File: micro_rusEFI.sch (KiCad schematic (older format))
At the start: 59 parts, among them J10 Conn_01x01, J11 Conn_01x01, J12 Conn_01x01, J13 Conn_01x01, J14 Conn_01x01, J16 Conn_01x01, J3 Conn_01x01, J4 Conn_02x05_Counter_Clockwise, J5 Conn_01x01, J6 Conn_01x01, J8 Conn_01x01, J9 Conn_01x01, U3 molex_48pin_MRE, U7 XC6206 3.3V

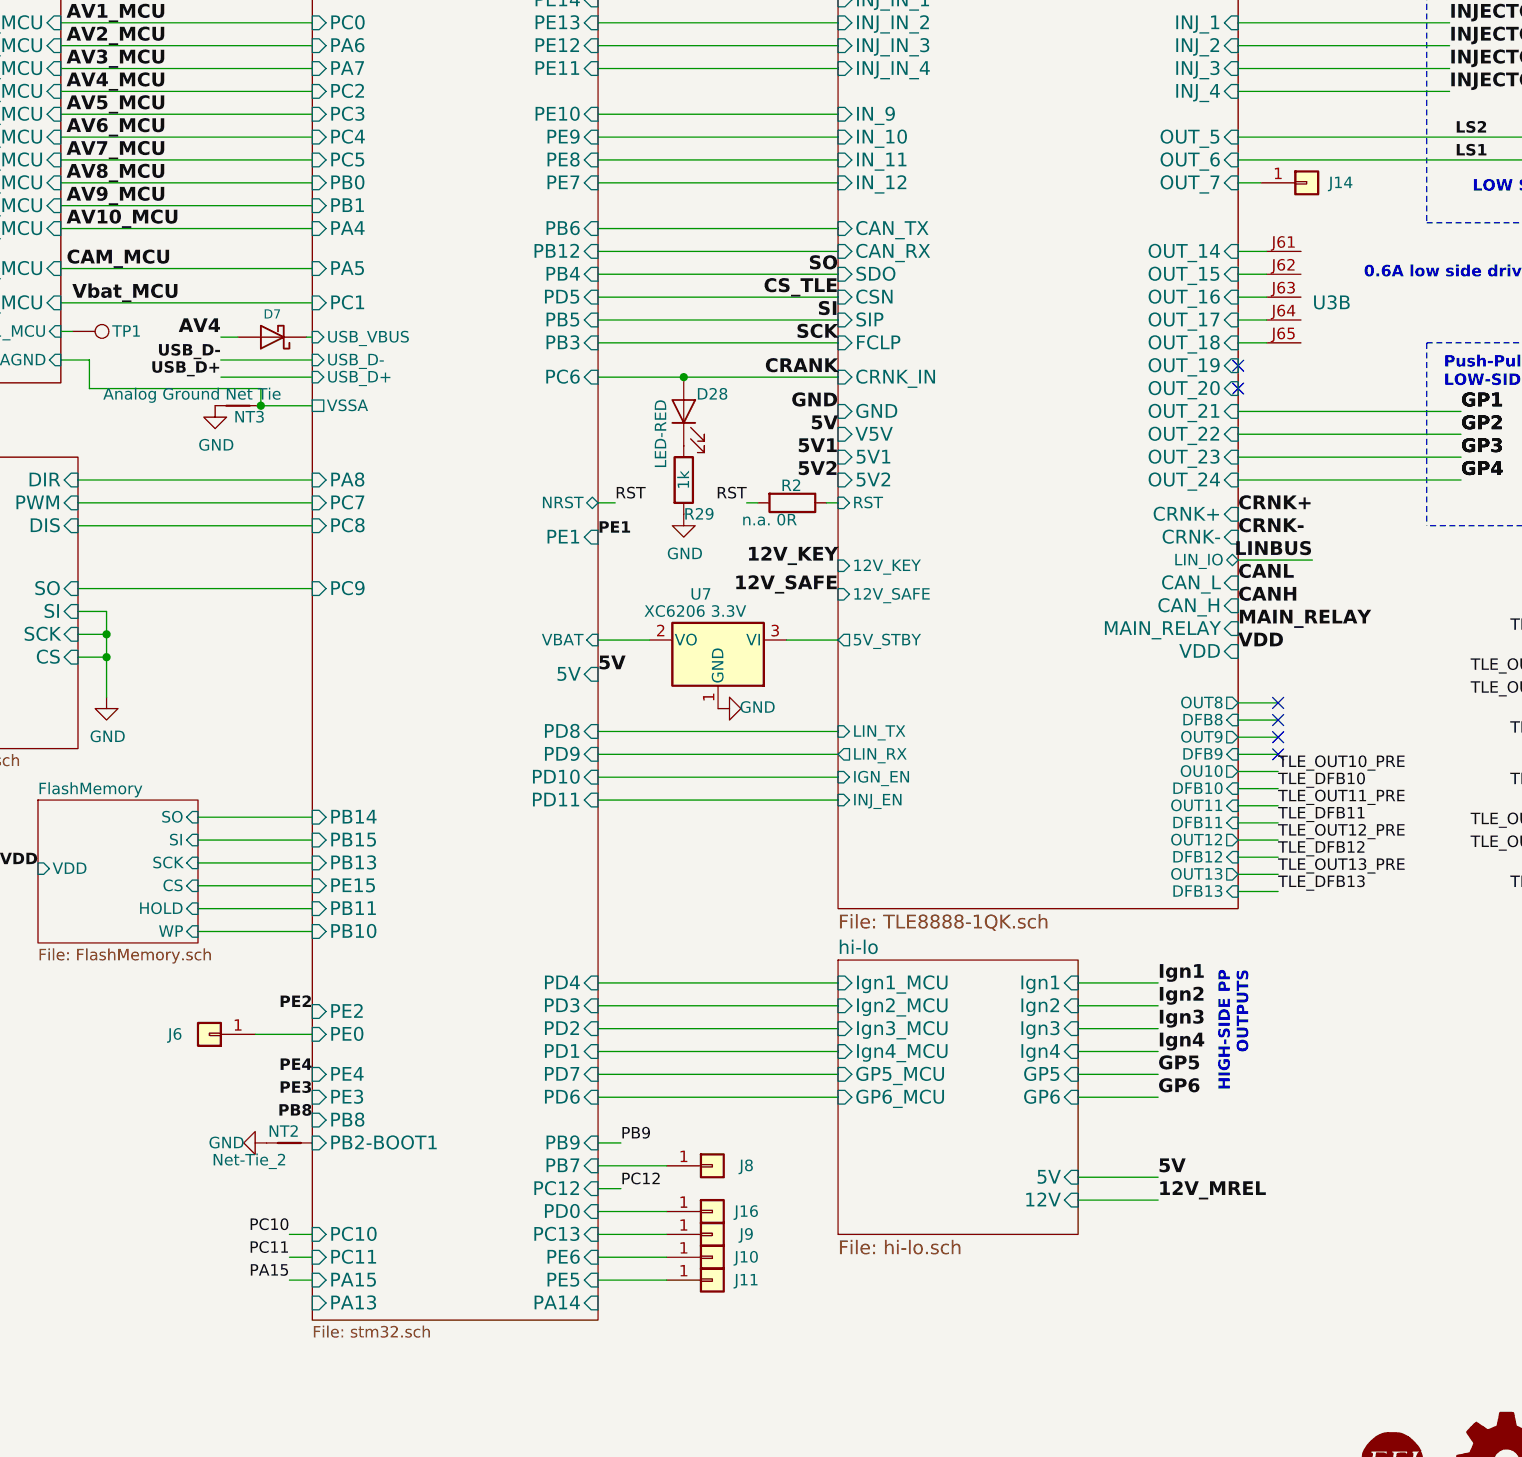
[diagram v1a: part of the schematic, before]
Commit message: Updated MRE footprint
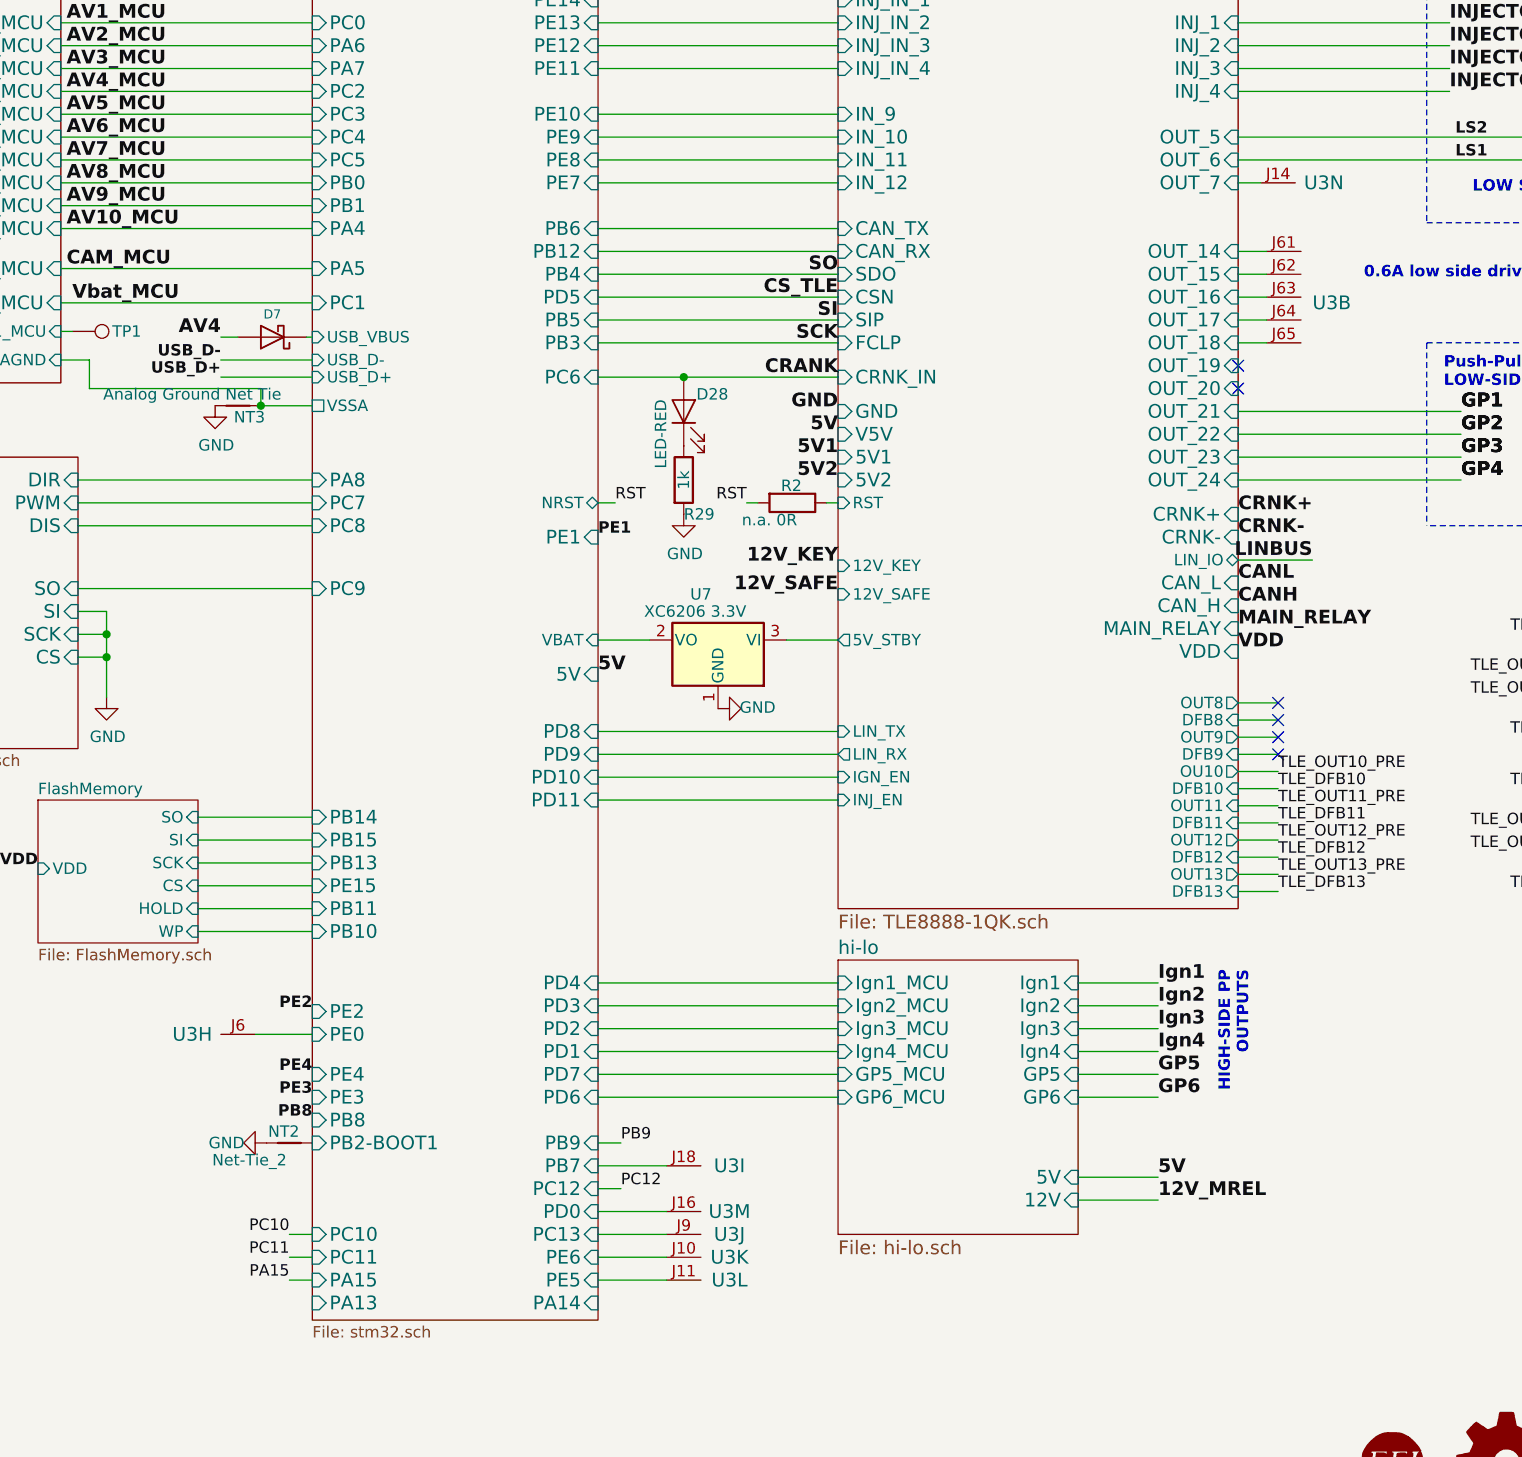
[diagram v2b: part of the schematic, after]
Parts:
- removed J10, J11, J14, J16, J6, J8, J9: Conn_01x01, Connector_Pin:Pin_D0.7mm_L6.5mm_W1.8mm_FlatFork, symbol Connector_Generic:Conn_01x01
- added unit 8 of U3
- added unit 9 of U3
- added unit 10 of U3
- added unit 11 of U3
- added unit 12 of U3
- added unit 13 of U3
- added unit 14 of U3
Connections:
- net MCU/PB7: now also U3.J18
- net MCU/PC13: now also U3.J9
- net MCU/PD0: now also U3.J16
- net MCU/PE0: now also U3.J6
- net MCU/PE5: now also U3.J11
- net MCU/PE6: now also U3.J10
- net TLE8888-1QK/OUT_7: now also U3.J14
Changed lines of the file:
@@
 F5 "OUT2" O R 13275 7550 50
 $EndSheet
-$Comp
-L Connector_Generic:Conn_01x01 J8
-U 1 1 5F20C313
-P 8450 8925
-F 0 "J8" H 8600 8925 50  0000 C CNN
-F 1 "Conn_01x01" H 8368 8791 50  0001 C CNN
-F 2 "Connector_Pin:Pin_D0.7mm_L6.5mm_W1.8mm_FlatFork" H 8450 8925 50  0001 C CNN
-F 3 "~" H 8450 8925 50  0001 C CNN
-	1    8450 8925
-	1    0    0    -1
-$EndComp
 Wire Wire Line
 	7950 8925 8250 8925
-$Comp
-L Connector_Generic:Conn_01x01 J6
-U 1 1 5F21FF07
-P 6250 8350
-F 0 "J6" H 6400 8350 50  0000 C CNN
-F 1 "Conn_01x01" H 6168 8216 50  0001 C CNN
-F 2 "Connector_Pin:Pin_D0.7mm_L6.5mm_W1.8mm_FlatFork" H 6250 8350 50  0001 C CNN
-F 3 "~" H 6250 8350 50  0001 C CNN
-	1    6250 8350
-	-1   0    0    1
-$EndComp
 Wire Wire Line
 	6700 8350 6450 8350
-$Comp
-L Connector_Generic:Conn_01x01 J10
-U 1 1 5F231677
-P 8450 9325
-F 0 "J10" H 8600 9325 50  0000 C CNN
-F 1 "Conn_01x01" H 8368 9191 50  0001 C CNN
-F 2 "Connector_Pin:Pin_D0.7mm_L6.5mm_W1.8mm_FlatFork" H 8450 9325 50  0001 C CNN
-F 3 "~" H 8450 9325 50  0001 C CNN
-	1    8450 9325
-	1    0    0    -1
-$EndComp
-$Comp
-L Connector_Generic:Conn_01x01 J11
-U 1 1 5F231C34
-P 8450 9425
-F 0 "J11" H 8600 9425 50  0000 C CNN
-F 1 "Conn_01x01" H 8368 9291 50  0001 C CNN
-F 2 "Connector_Pin:Pin_D0.7mm_L6.5mm_W1.8mm_FlatFork" H 8450 9425 50  0001 C CNN
-F 3 "~" H 8450 9425 50  0001 C CNN
-	1    8450 9425
-	1    0    0    -1
-$EndComp
 Wire Wire Line
 	7950 9325 8250 9325
 Wire Wire Line
 	7950 9425 8250 9425
-$Comp
-L Connector_Generic:Conn_01x01 J9
-U 1 1 5F2548AA
-P 8450 9225
-F 0 "J9" H 8600 9225 50  0000 C CNN
-F 1 "Conn_01x01" H 8368 9091 50  0001 C CNN
-F 2 "Connector_Pin:Pin_D0.7mm_L6.5mm_W1.8mm_FlatFork" H 8450 9225 50  0001 C CNN
-F 3 "~" H 8450 9225 50  0001 C CNN
-	1    8450 9225
-	1    0    0    -1
-$EndComp
 Wire Wire Line
 	7950 9225 8250 9225
@@
 Wire Wire Line
 	13275 5125 13275 5025
-$Comp
-L Connector_Generic:Conn_01x01 J16
-U 1 1 5F3E511F
-P 8450 9125
-F 0 "J16" H 8600 9125 50  0000 C CNN
-F 1 "Conn_01x01" H 8368 8991 50  0001 C CNN
-F 2 "Connector_Pin:Pin_D0.7mm_L6.5mm_W1.8mm_FlatFork" H 8450 9125 50  0001 C CNN
-F 3 "~" H 8450 9125 50  0001 C CNN
-	1    8450 9125
-	1    0    0    -1
-$EndComp
 Wire Wire Line
 	7950 9125 8250 9125
@@
 Wire Wire Line
 	8600 6025 8650 6025
-$Comp
-L Connector_Generic:Conn_01x01 J14
-U 1 1 5EF49354
-P 11050 4625
-F 0 "J14" H 11200 4625 50  0000 C CNN
-F 1 "Conn_01x01" H 10968 4491 50  0001 C CNN
-F 2 "Connector_Pin:Pin_D0.7mm_L6.5mm_W1.8mm_FlatFork" H 11050 4625 50  0001 C CNN
-F 3 "~" H 11050 4625 50  0001 C CNN
-	1    11050 4625
-	1    0    0    -1
-$EndComp
 Wire Wire Line
 	10750 4625 10850 4625
@@
 	1    0    0    -1
 $EndComp
+$Comp
+L rusefi_Molex_MRE_Connector:molex_48pin_MRE U3
+U 8 1 5FDEA88F
+P 7000 8350
+F 0 "U3" H 7825 8350 60  0000 C CNN
+F 1 "molex_48pin_MRE" V 8181 8755 60  0001 C CNN
+F 2 "rusefi_lib:Molex_48_MRE" H 7000 8350 60  0001 C CNN
+F 3 "" H 7000 8350 60  0001 C CNN
+	8    7000 8350
+	-1   0    0    1
+$EndComp
+$Comp
+L rusefi_Molex_MRE_Connector:molex_48pin_MRE U3
+U 9 1 5FE1BBB9
+P 7700 8925
+F 0 "U3" H 8525 8925 60  0000 C CNN
+F 1 "molex_48pin_MRE" V 8881 9330 60  0001 C CNN
+F 2 "rusefi_lib:Molex_48_MRE" H 7700 8925 60  0001 C CNN
+F 3 "" H 7700 8925 60  0001 C CNN
+	9    7700 8925
+	1    0    0    -1
+$EndComp
+$Comp
+L rusefi_Molex_MRE_Connector:molex_48pin_MRE U3
+U 10 1 5FE33973
+P 7700 9225
+F 0 "U3" H 8525 9225 60  0000 C CNN
+F 1 "molex_48pin_MRE" V 8881 9630 60  0001 C CNN
+F 2 "rusefi_lib:Molex_48_MRE" H 7700 9225 60  0001 C CNN
+F 3 "" H 7700 9225 60  0001 C CNN
+	10   7700 9225
+	1    0    0    -1
+$EndComp
+$Comp
+L rusefi_Molex_MRE_Connector:molex_48pin_MRE U3
+U 11 1 5FE3397D
+P 7700 9325
+F 0 "U3" H 8525 9325 60  0000 C CNN
+F 1 "molex_48pin_MRE" V 8881 9730 60  0001 C CNN
+F 2 "rusefi_lib:Molex_48_MRE" H 7700 9325 60  0001 C CNN
+F 3 "" H 7700 9325 60  0001 C CNN
+	11   7700 9325
+	1    0    0    -1
+$EndComp
+$Comp
+L rusefi_Molex_MRE_Connector:molex_48pin_MRE U3
+U 12 1 5FE4FA20
+P 7700 9425
+F 0 "U3" H 8525 9425 60  0000 C CNN
+F 1 "molex_48pin_MRE" V 8881 9830 60  0001 C CNN
+F 2 "rusefi_lib:Molex_48_MRE" H 7700 9425 60  0001 C CNN
+F 3 "" H 7700 9425 60  0001 C CNN
+	12   7700 9425
+	1    0    0    -1
+$EndComp
+$Comp
+L rusefi_Molex_MRE_Connector:molex_48pin_MRE U3
+U 13 1 5FE4FA2A
+P 7700 9125
+F 0 "U3" H 8525 9125 60  0000 C CNN
+F 1 "molex_48pin_MRE" V 8881 9530 60  0001 C CNN
+F 2 "rusefi_lib:Molex_48_MRE" H 7700 9125 60  0001 C CNN
+F 3 "" H 7700 9125 60  0001 C CNN
+	13   7700 9125
+	1    0    0    -1
+$EndComp
+$Comp
+L rusefi_Molex_MRE_Connector:molex_48pin_MRE U3
+U 14 1 5FE4FA34
+P 10300 4625
+F 0 "U3" H 11125 4625 60  0000 C CNN
+F 1 "molex_48pin_MRE" V 11481 5030 60  0001 C CNN
+F 2 "rusefi_lib:Molex_48_MRE" H 10300 4625 60  0001 C CNN
+F 3 "" H 10300 4625 60  0001 C CNN
+	14   10300 4625
+	1    0    0    -1
+$EndComp

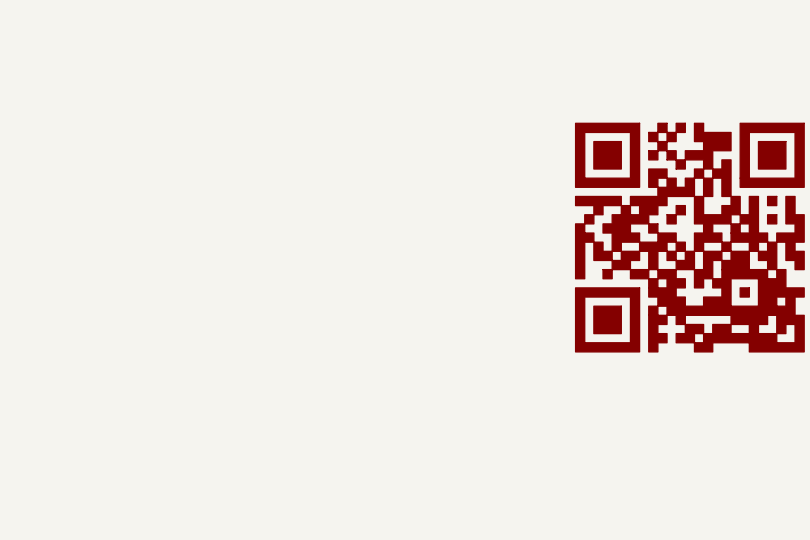
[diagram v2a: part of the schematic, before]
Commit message: Added disclaimer silk screen and schematic note.
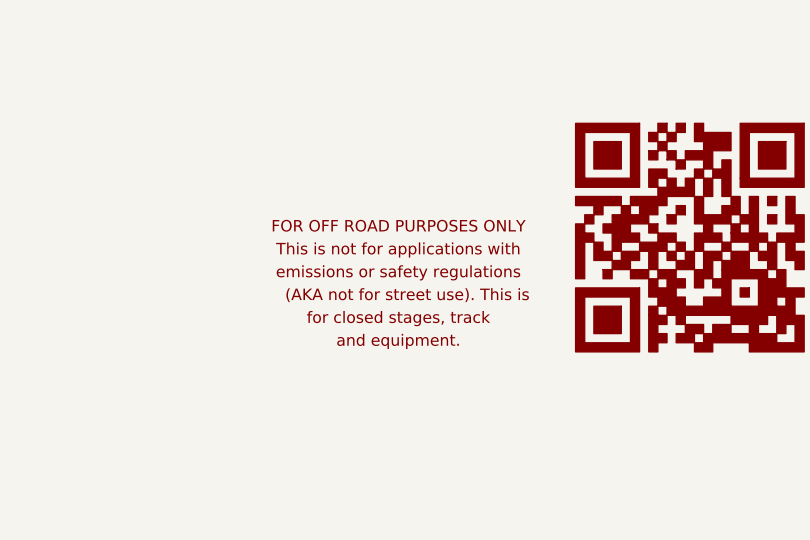
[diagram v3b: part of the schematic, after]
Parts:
- added G1: Disclaimer, rusefi_lib:Off_Road_Disclaimer, symbol Off_Road_Disclaimer:Disclaimer
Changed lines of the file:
@@
+	1    0    0    -1
+$EndComp
+$Comp
+L Off_Road_Disclaimer:Disclaimer G1
+U 1 1 5F63E1FA
+P 14600 9250
+F 0 "G1" H 14600 9600 60  0001 C CNN
+F 1 "Disclaimer" H 14600 9500 60  0001 C CNN
+F 2 "rusefi_lib:Off_Road_Disclaimer" H 14600 9250 50  0001 C CNN
+F 3 "" H 14600 9250 50  0001 C CNN
+	1    14600 9250
 	1    0    0    -1
 $EndComp
